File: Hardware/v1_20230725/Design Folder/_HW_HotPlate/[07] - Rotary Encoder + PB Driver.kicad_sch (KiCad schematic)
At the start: 15 parts, among them J701 RCPT_5POS_2.54MM_RA, U701 SN74LVC1G17DBVR, U702 SN74LVC1G17DBVR, U703 DLPT05A-7, U704 SN74LVC1G17DBVR

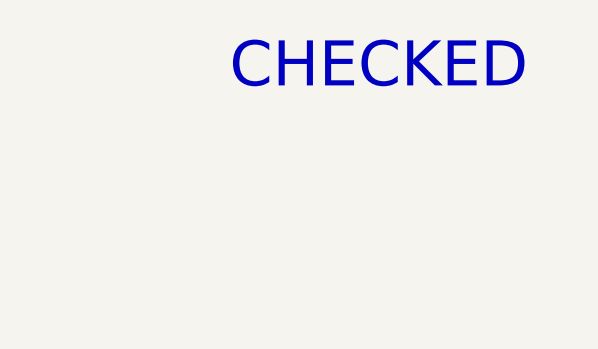
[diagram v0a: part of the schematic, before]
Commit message: Schematic library has been updated
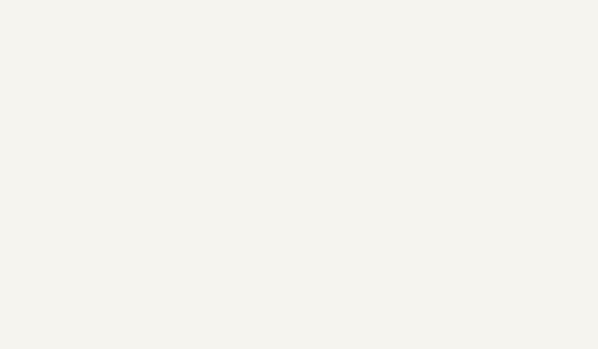
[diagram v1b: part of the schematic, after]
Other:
- note removed: "CHECKED"
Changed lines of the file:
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@@
 (kicad_sch (version 20230121) (generator eeschema)
-  (paper "B")
+  (paper "C")
   (title_block
     (title "Hot Plate")
@@
     (company "Mend0z0")
     (comment 1 "v1")
+    (comment 2 "RELEASED")
     (comment 3 "Siavash Taher Parvar")
     (comment 8 "N/A")
@@
     (stroke (width 0) (type default))
   )
-  (text "CHECKED" (at 378.46 34.29 0)
-    (effects (font (size 5 5)) (justify left bottom))
-  )
   (label "KEY-040_B" (at 83.82 148.59 0) (fields_autoplaced)

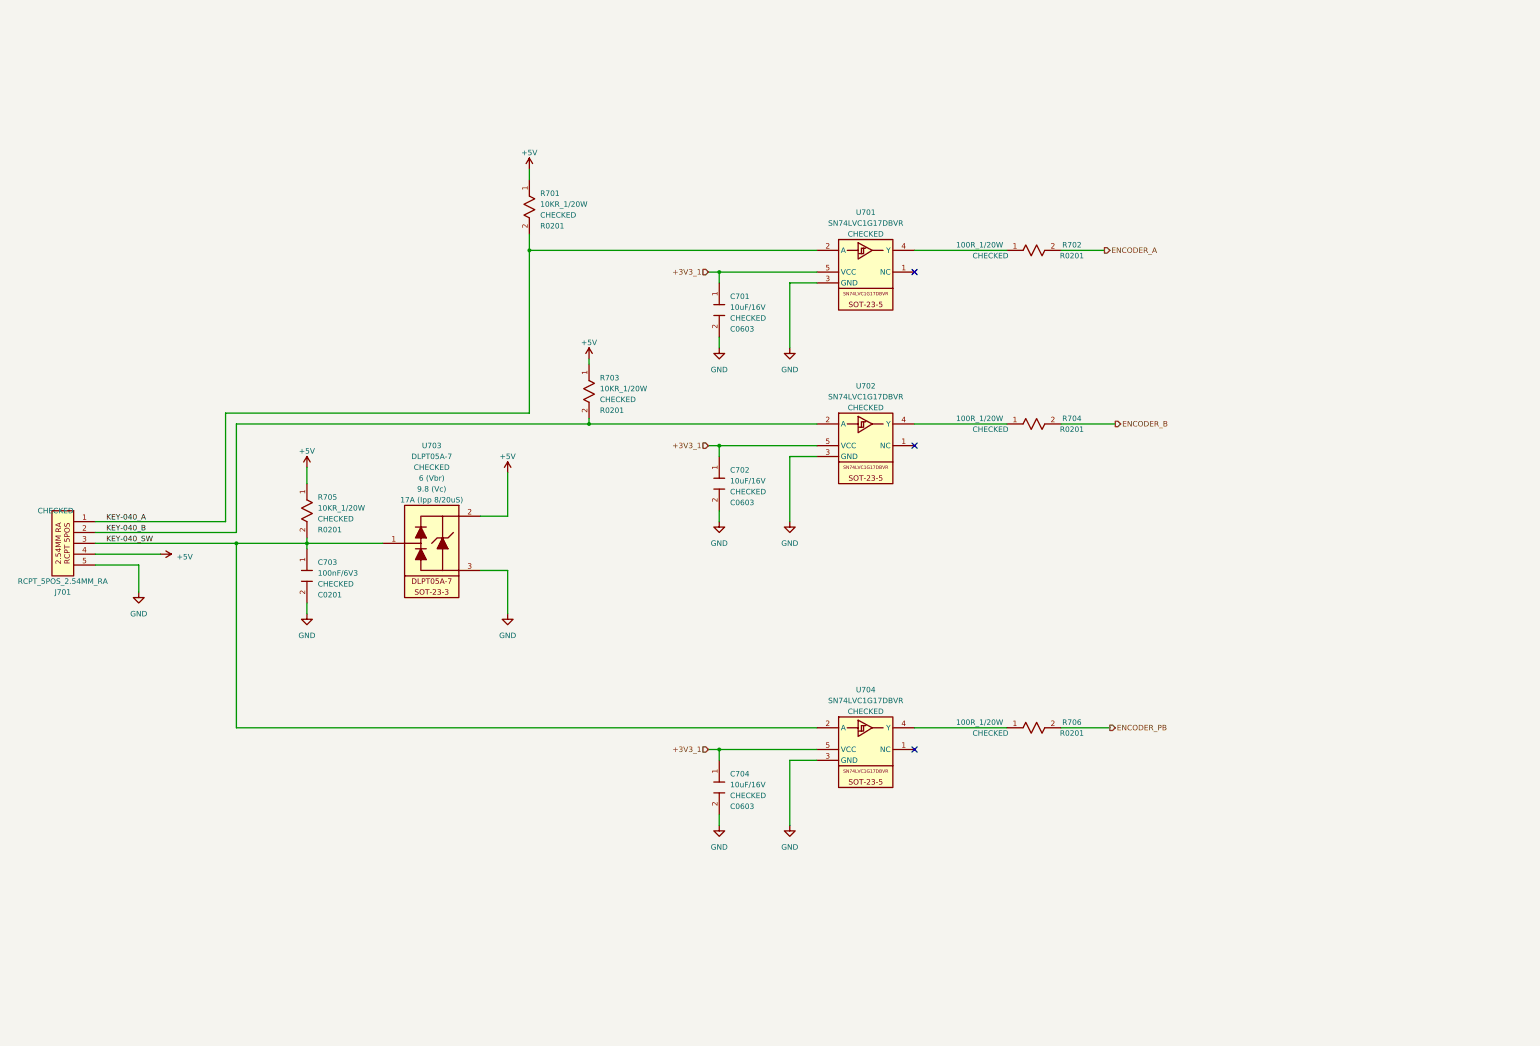
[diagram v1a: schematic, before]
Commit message: components have been updated
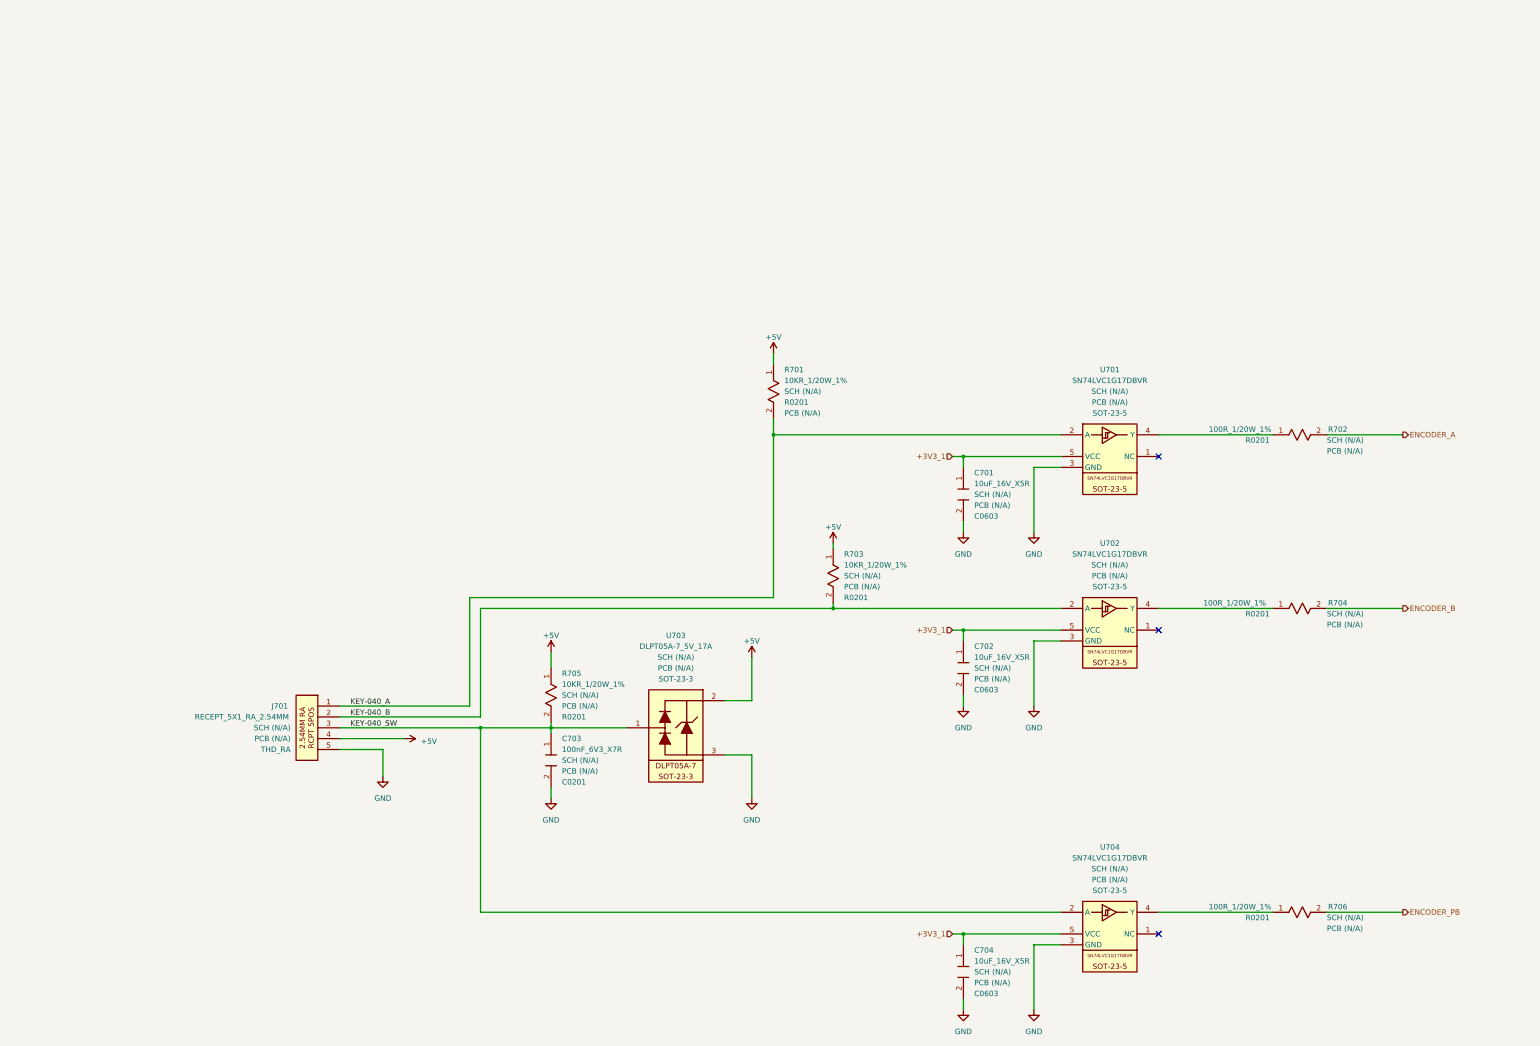
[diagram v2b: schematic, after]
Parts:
- C701, C702, C704: value 10uF/16V -> 10uF_16V_X5R; symbol _SCHLIB_HotPlate:CAP_10uF/16V-C0603 -> _SCHLIB_HotPlate:CAP_10uF_16V_X5R_C0603; Manufacturer (none) -> Murata Electronics; PCB CHECk (none) -> PCB (N/A); Part Number GRT188R61C106KE13J -> (none); Part Number (Manufacturer) (none) -> GRT188R61C106KE13J; Part Number (Vendor) (none) -> 490-GRT188R61C106KE13JTR-ND; SCH CHECK CHECKED -> SCH (N/A); Vendor (none) -> Digikey
- C703: value 100nF/6V3 -> 100nF_6V3_X7R; symbol _SCHLIB_HotPlate:CAP_100nF/6V3_C0201 -> _SCHLIB_HotPlate:CAP_100nF_6V3_X7R_C0201; Manufacturer (none) -> YAGEO; PCB CHECk (none) -> PCB (N/A); Part Number CC0201KRX7R5BB104 -> (none); Part Number (Manufacturer) (none) -> CC0201KRX7R5BB104; Part Number (Vendor) (none) -> 13-CC0201KRX7R5BB104TR-ND; SCH CHECK CHECKED -> SCH (N/A); Vendor (none) -> Digikey
- J701: value RCPT_5POS_2.54MM_RA -> RECEPT_5X1_RA_2.54MM; symbol _SCHLIB_HotPlate:CONN_RCPT_5POS_2.54MM_RA -> _SCHLIB_HotPlate:CONN_RECEPT_5POS_RA_2.54MM; Manufacturer (none) -> Sullins Connector Solutions; PCB CHECk (none) -> PCB (N/A); Package (none) -> THD_RA; Part Number PPTC051LGBN-RC -> (none); Part Number (Manufacturer) (none) -> PPTC051LGBN-RC; Part Number (Vendor) (none) -> S5441-ND; SCH CHECK CHECKED -> SCH (N/A); Vendor (none) -> Digikey
- R701, R703, R705: value 10KR_1/20W -> 10KR_1/20W_1%; symbol _SCHLIB_HotPlate:RES_10KR_1/20W-R0201 -> _SCHLIB_HotPlate:RES_10KR_1/20W_1%_R0201; Manufacturer (none) -> Stackpole Electronics Inc; PCB CHECk (none) -> PCB (N/A); Part Number RMCF0201FT10K0 -> (none); Part Number (Manufacturer) (none) -> RMCF0201FT10K0; Part Number (Vendor) (none) -> RMCF0201FT10K0TR-ND; SCH CHECK CHECKED -> SCH (N/A); Vendor (none) -> Digikey
- R702, R704, R706: value 100R_1/20W -> 100R_1/20W_1%; symbol _SCHLIB_HotPlate:RES_100R_1/20W-R0201 -> _SCHLIB_HotPlate:RES_100R_1/20W_1%_R0201; Manufacturer (none) -> Stackpole Electronics Inc; PCB CHECk (none) -> PCB (N/A); Part Number RMCF0201FT100R -> (none); Part Number (Manufacturer) (none) -> RMCF0201FT100R; Part Number (Vendor) (none) -> RMCF0201FT100RTR-ND; SCH CHECK CHECKED -> SCH (N/A); Vendor (none) -> Digikey
- U701, U702, U704: symbol _SCHLIB_HotPlate:BUF_SN74LVC1G17DBVR_SOT-23-5 -> _SCHLIB_HotPlate:IC_BUFFER_SN74LVC1G17DBVR_NON-INV_5.5V_32mA_SOT-23-5; Manufacturer (none) -> Texas Instruments; PCB CHECk (none) -> PCB (N/A); Package (none) -> SOT-23-5; Part Number SN74LVC1G17DBVR -> (none); Part Number (Manufacturer) (none) -> SN74LVC1G17DBVR; Part Number (Vendor) (none) -> 296-11933-2-ND; SCH CHECK CHECKED -> SCH (N/A); Vendor (none) -> Digikey
- U703: value DLPT05A-7 -> DLPT05A-7_5V_17A; symbol _SCHLIB_HotPlate:TVS_DLPT05A-7_SOT_23 -> _SCHLIB_HotPlate:DIODE_TVS_DLPT05A-7_5V_6V_17A(8/20us)_SOT_23; Ipp 17A (Ipp 8/20uS) -> (none); Manufacturer (none) -> Diodes Incorporated; PCB CHECk (none) -> PCB (N/A); Package (none) -> SOT-23-3; Part Number DLPT05A-7 -> (none); Part Number (Manufacturer) (none) -> DLPT05A-7; Part Number (Vendor) (none) -> 31-DLPT05A-7TR-ND; SCH CHECK CHECKED -> SCH (N/A); Vbr 6 (Vbr) -> (none); Vc 9.8 (Vc) -> (none); Vendor (none) -> Digikey
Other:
- moved on the sheet: C701, C702, C703, C704, J701, R701, R702, R703, R704, R705, R706, U701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
